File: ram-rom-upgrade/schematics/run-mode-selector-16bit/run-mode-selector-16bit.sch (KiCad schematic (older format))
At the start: 16 parts

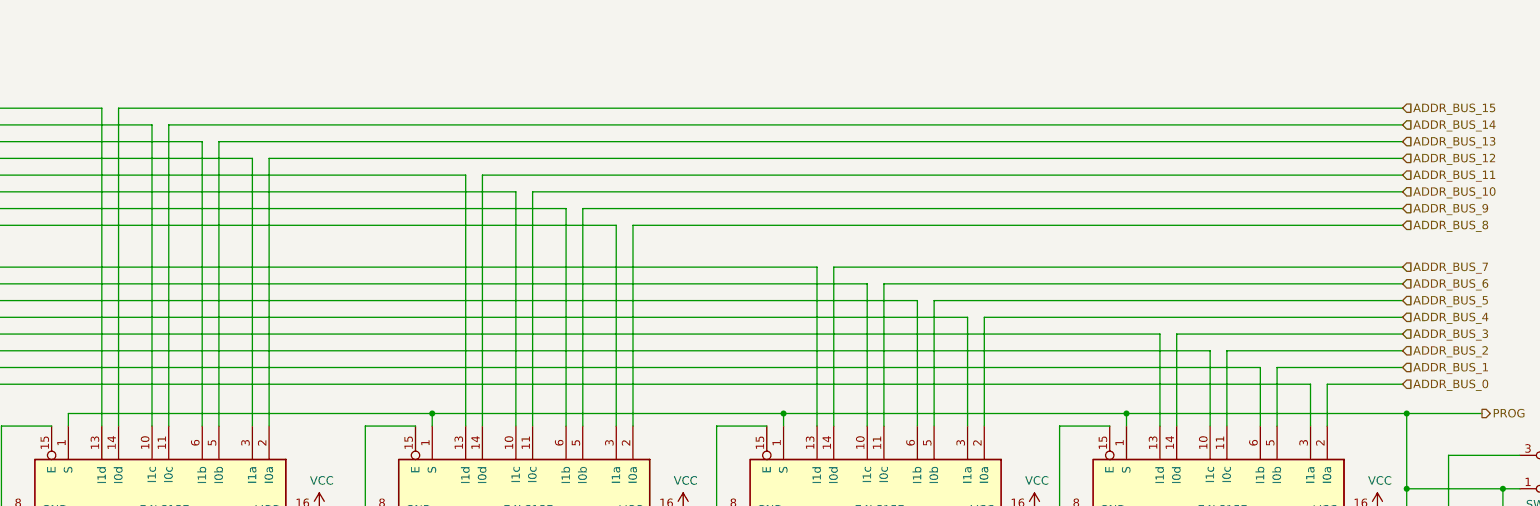
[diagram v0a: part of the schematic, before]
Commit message: added pull down resistors
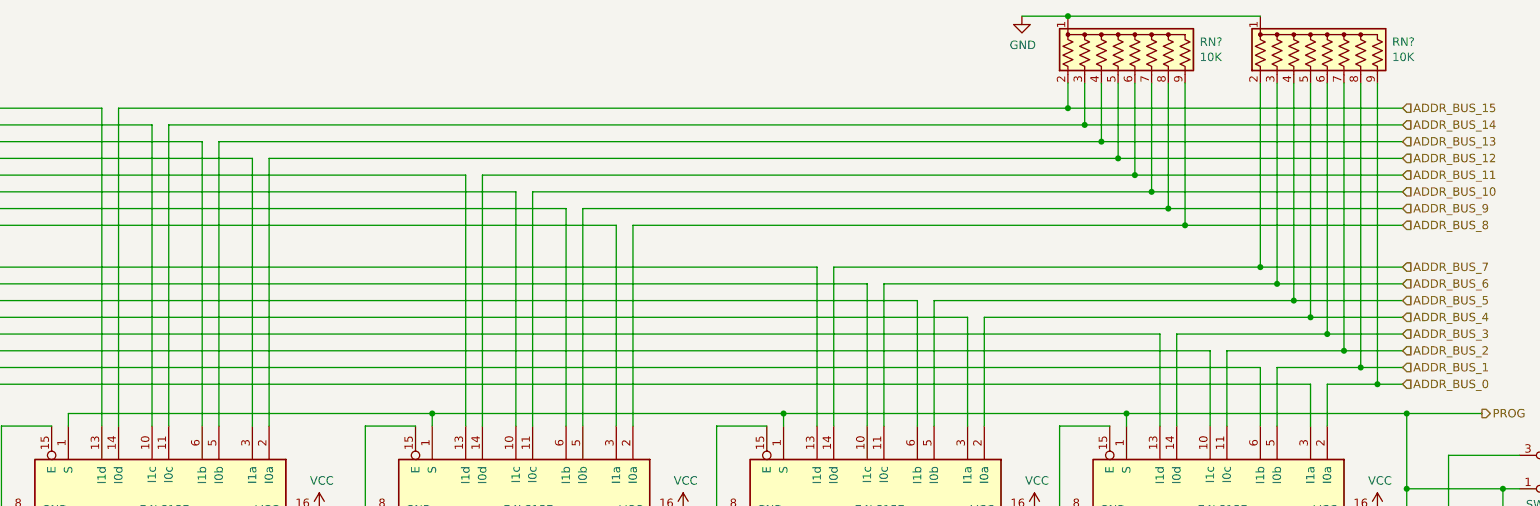
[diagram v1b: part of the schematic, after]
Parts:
- added RN? (x2): 10K, Resistor_THT:R_Array_SIP9, symbol Device:R_Network08_US
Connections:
- net ADDR_BUS_0: now also RN?.9 (R8)
- net ADDR_BUS_1: now also RN?.8 (R7)
- net ADDR_BUS_10: now also RN?.7 (R6)
- net ADDR_BUS_11: now also RN?.6 (R5)
- net ADDR_BUS_12: now also RN?.5 (R4)
- net ADDR_BUS_13: now also RN?.4 (R3)
- net ADDR_BUS_14: now also RN?.3 (R2)
- net ADDR_BUS_15: now also RN?.2 (R1)
- net ADDR_BUS_2: now also RN?.7 (R6)
- net ADDR_BUS_3: now also RN?.6 (R5)
- net ADDR_BUS_4: now also RN?.5 (R4)
- net ADDR_BUS_5: now also RN?.4 (R3)
- net ADDR_BUS_6: now also RN?.3 (R2)
- net ADDR_BUS_7: now also RN?.2 (R1)
- net ADDR_BUS_8: now also RN?.9 (R8)
- net ADDR_BUS_9: now also RN?.8 (R7)
- net GND: now also RN?.1 (common), RN?.1 (common)
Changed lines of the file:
@@
 	9450 3650 9450 3400
 Wire Wire Line
-	9450 3400 9900 3400
+	9450 3400 9750 3400
 Wire Wire Line
 	9150 3650 9150 3300
 Wire Wire Line
-	9150 3300 9900 3300
-Wire Wire Line
-	8850 3200 9900 3200
-Wire Wire Line
-	8550 3100 9900 3100
+	9150 3300 9650 3300
+Wire Wire Line
+	8850 3200 9550 3200
+Wire Wire Line
+	8550 3100 9450 3100
 Wire Wire Line
 	7400 3650 7400 3000
 Wire Wire Line
-	7400 3000 9900 3000
+	7400 3000 9350 3000
 Wire Wire Line
 	7100 3650 7100 2900
 Wire Wire Line
-	7100 2900 9900 2900
-Wire Wire Line
-	6800 2800 9900 2800
-Wire Wire Line
-	6500 2700 9900 2700
+	7100 2900 9250 2900
+Wire Wire Line
+	6800 2800 9150 2800
+Wire Wire Line
+	6500 2700 9050 2700
 Wire Wire Line
 	5300 3650 5300 2450
 Wire Wire Line
-	5300 2450 9900 2450
+	5300 2450 8600 2450
 Wire Wire Line
 	5000 3650 5000 2350
 Wire Wire Line
-	5000 2350 9900 2350
-Wire Wire Line
-	4700 2250 9900 2250
-Wire Wire Line
-	4400 2150 9900 2150
+	5000 2350 8500 2350
+Wire Wire Line
+	4700 2250 8400 2250
+Wire Wire Line
+	4400 2150 8300 2150
 Wire Wire Line
 	3125 3650 3125 2050
 Wire Wire Line
-	3125 2050 9900 2050
+	3125 2050 8200 2050
 Wire Wire Line
 	2825 3650 2825 1950
 Wire Wire Line
-	2825 1950 9900 1950
+	2825 1950 8100 1950
 Wire Wire Line
 	2525 3650 2525 1850
 Wire Wire Line
-	2525 1850 9900 1850
-Wire Wire Line
-	2225 1750 9900 1750
+	2525 1850 8000 1850
+Wire Wire Line
+	2225 1750 7900 1750
 $Comp
 L ram-rom-upgrade-symbols:BarGraphLED_8P BAR?
@@
 	1    0    0    -1
 $EndComp
+$Comp
+L Device:R_Network08_US RN?
+U 1 1 60736850
+P 9450 1400
+F 0 "RN?" H 9838 1446 50  0000 L CNN
+F 1 "10K" H 9838 1355 50  0000 L CNN
+F 2 "Resistor_THT:R_Array_SIP9" V 9925 1400 50  0001 C CNN
+F 3 "http://www.vishay.com/docs/31509/csc.pdf" H 9450 1400 50  0001 C CNN
+	1    9450 1400
+	1    0    0    -1
+$EndComp
+$Comp
+L Device:R_Network08_US RN?
+U 1 1 6073A7C3
+P 8300 1400
+F 0 "RN?" H 8688 1446 50  0000 L CNN
+F 1 "10K" H 8688 1355 50  0000 L CNN
+F 2 "Resistor_THT:R_Array_SIP9" V 8775 1400 50  0001 C CNN
+F 3 "http://www.vishay.com/docs/31509/csc.pdf" H 8300 1400 50  0001 C CNN
+	1    8300 1400
+	1    0    0    -1
+$EndComp
+Wire Wire Line
+	9750 1600 9750 3400
+Connection ~ 9750 3400
+Wire Wire Line
+	9750 3400 9900 3400
+Wire Wire Line
+	9650 1600 9650 3300
+Connection ~ 9650 3300
+Wire Wire Line
+	9650 3300 9900 3300
+Wire Wire Line
+	9550 1600 9550 3200
+Connection ~ 9550 3200
+Wire Wire Line
+	9550 3200 9900 3200
+Wire Wire Line
+	9450 1600 9450 3100
+Connection ~ 9450 3100
+Wire Wire Line
+	9450 3100 9900 3100
+Wire Wire Line
+	9350 1600 9350 3000
+Connection ~ 9350 3000
+Wire Wire Line
+	9350 3000 9900 3000
+Wire Wire Line
+	9250 1600 9250 2900
+Connection ~ 9250 2900
+Wire Wire Line
+	9250 2900 9900 2900
+Wire Wire Line
+	9150 1600 9150 2800
+Connection ~ 9150 2800
+Wire Wire Line
+	9150 2800 9900 2800
+Wire Wire Line
+	9050 1600 9050 2700
+Connection ~ 9050 2700
+Wire Wire Line
+	9050 2700 9900 2700
+Wire Wire Line
+	8600 1600 8600 2450
+Connection ~ 8600 2450
+Wire Wire Line
+	8600 2450 9900 2450
+Wire Wire Line
+	8500 1600 8500 2350
+Connection ~ 8500 2350
+Wire Wire Line
+	8500 2350 9900 2350
+Wire Wire Line
+	8400 1600 8400 2250
+Connection ~ 8400 2250
+Wire Wire Line
+	8400 2250 9900 2250
+Wire Wire Line
+	8300 1600 8300 2150
+Connection ~ 8300 2150
+Wire Wire Line
+	8300 2150 9900 2150
+Wire Wire Line
+	8200 1600 8200 2050
+Connection ~ 8200 2050
+Wire Wire Line
+	8200 2050 9900 2050
+Wire Wire Line
+	8100 1600 8100 1950
+Connection ~ 8100 1950
+Wire Wire Line
+	8100 1950 9900 1950
+Wire Wire Line
+	8000 1600 8000 1850
+Connection ~ 8000 1850
+Wire Wire Line
+	8000 1850 9900 1850
+Wire Wire Line
+	7900 1600 7900 1750
+Connection ~ 7900 1750
+Wire Wire Line
+	7900 1750 9900 1750
+Wire Wire Line
+	9050 1200 7900 1200
+$Comp
+L power:GND #PWR?
+U 1 1 60809B64
+P 7625 1200
+F 0 "#PWR?" H 7625 950 50  0001 C CNN
+F 1 "GND" H 7630 1027 50  0000 C CNN
+F 2 "" H 7625 1200 50  0001 C CNN
+F 3 "" H 7625 1200 50  0001 C CNN
+	1    7625 1200
+	1    0    0    -1
+$EndComp
+Wire Wire Line
+	7900 1200 7625 1200
+Connection ~ 7900 1200
 $EndSCHEMATC

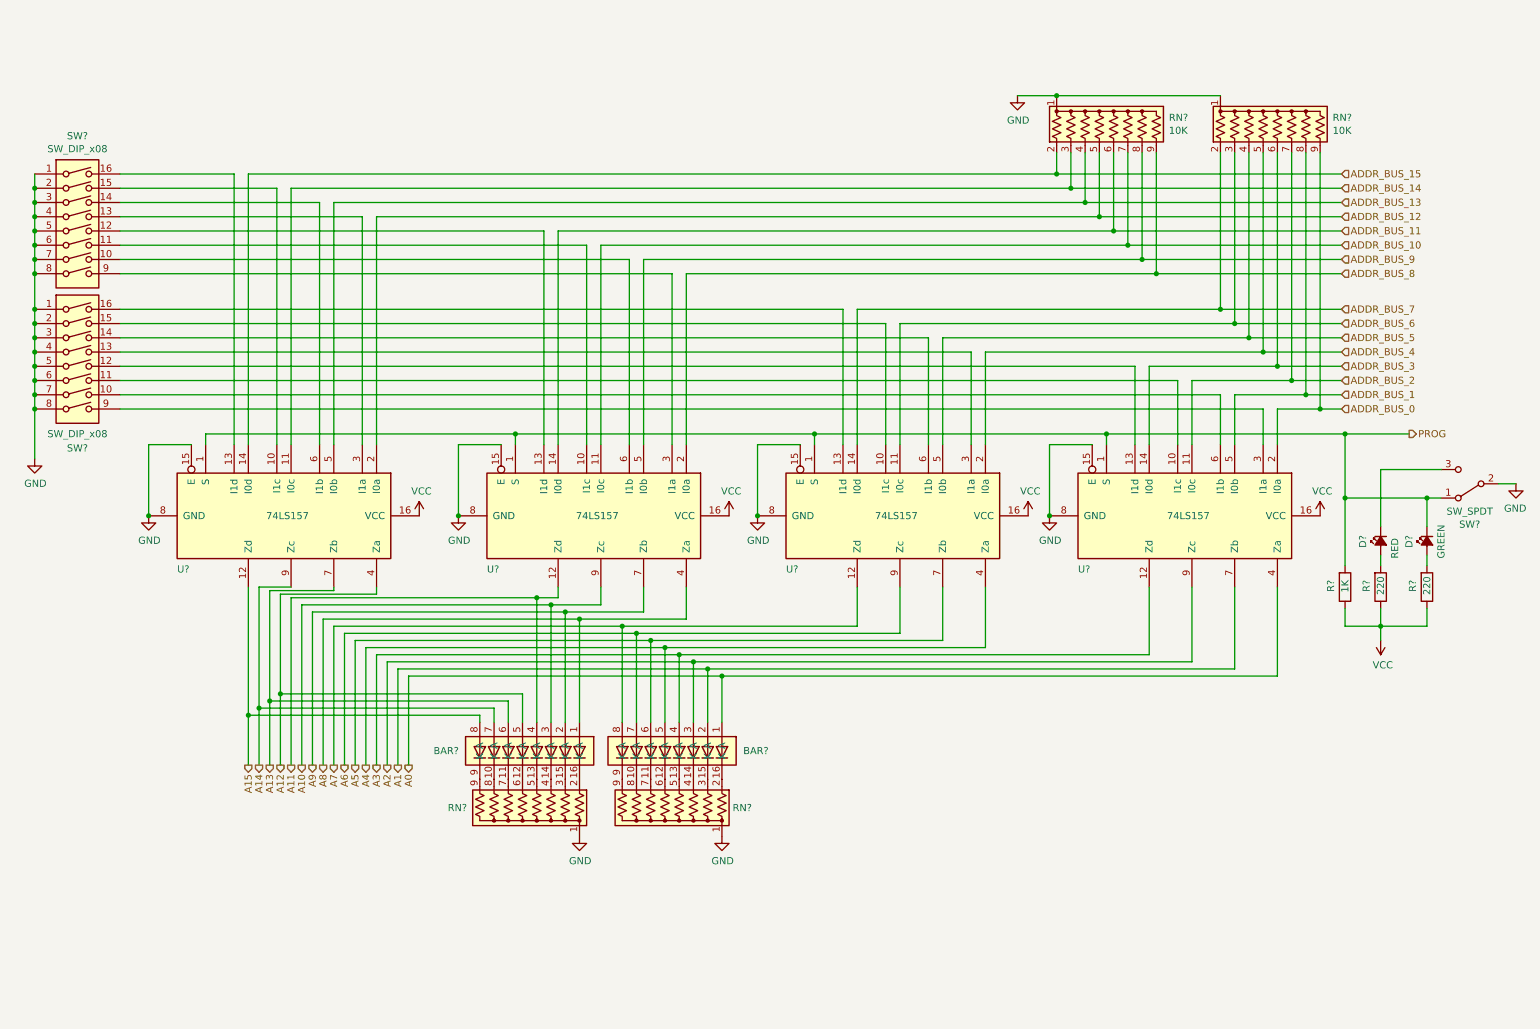
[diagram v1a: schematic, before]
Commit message: added transceiver from address to data bus
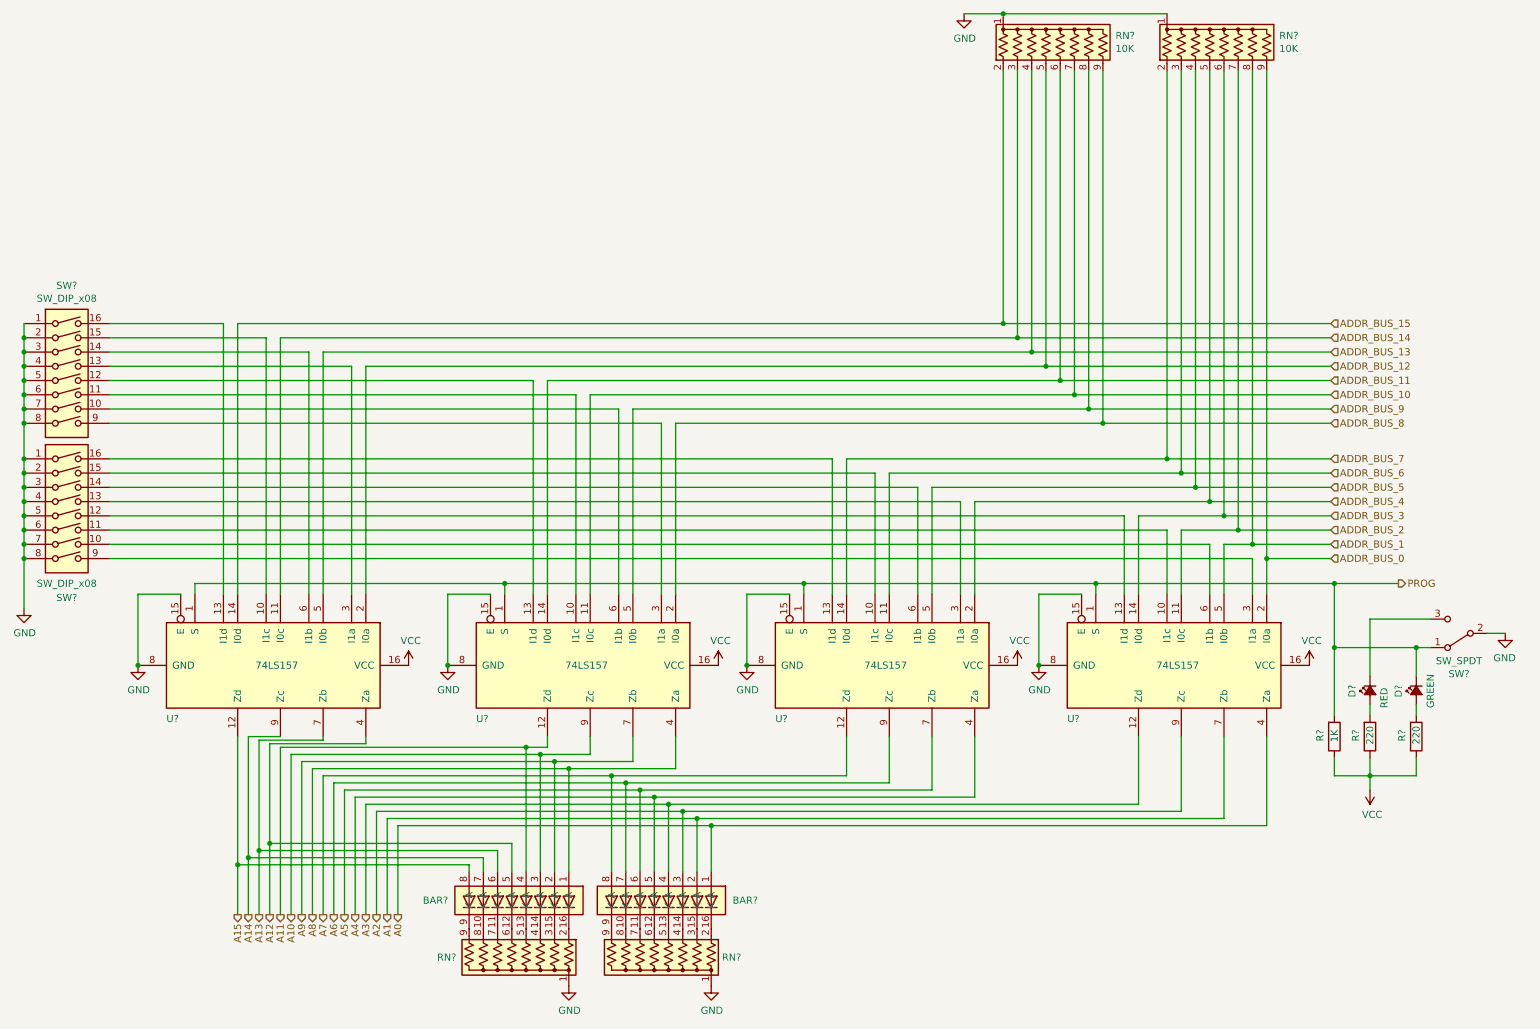
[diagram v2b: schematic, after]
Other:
- moved on the sheet: BAR?, D?, R?, RN?, SW?, U?
